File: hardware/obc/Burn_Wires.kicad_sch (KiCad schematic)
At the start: 28 parts, among them Q501 MMBT2222AT, Q502 IRLML2803, Q503 IRLML2803, Q504 IRLML2803, Q505 IRF7406PbF, Q506 IRF7406PbF, Q507 IRF7406PbF, U501 PE014006

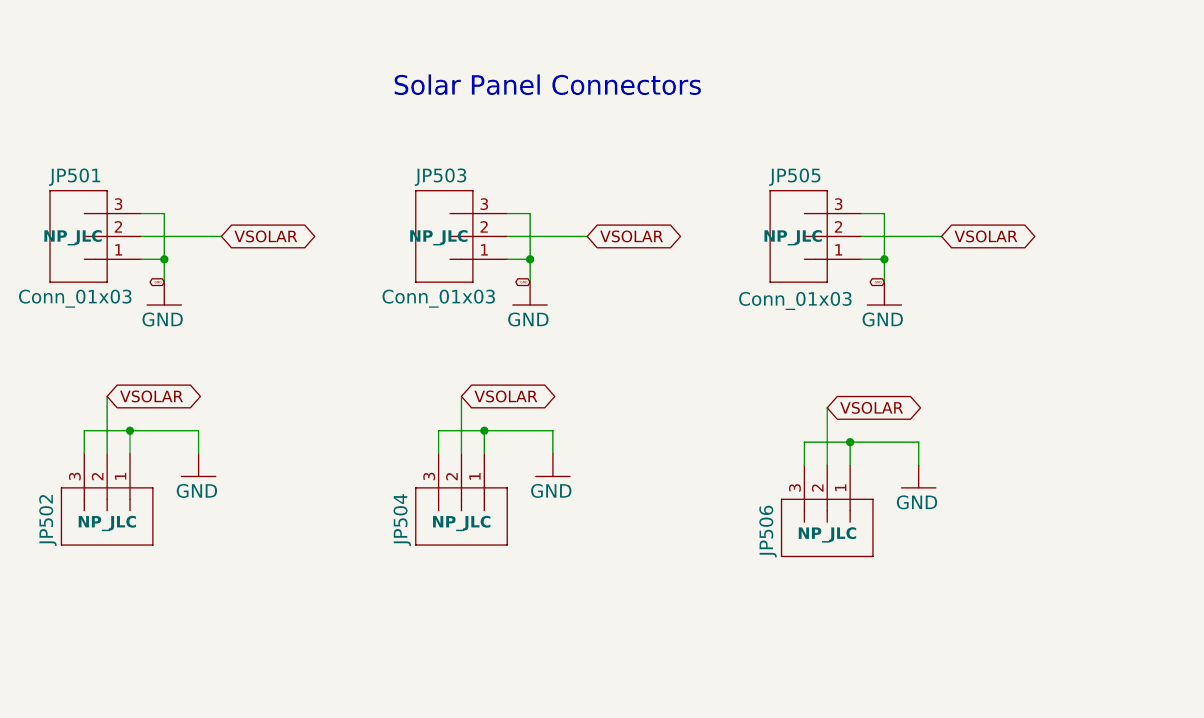
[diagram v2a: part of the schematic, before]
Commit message: OBC; Added another solar charger
- completed all RP2350B decoupling
- added all footprints for new parts
- created a new sheet for all solar charging components
	- added another solar chager to accomadate more voltage from solar pannels
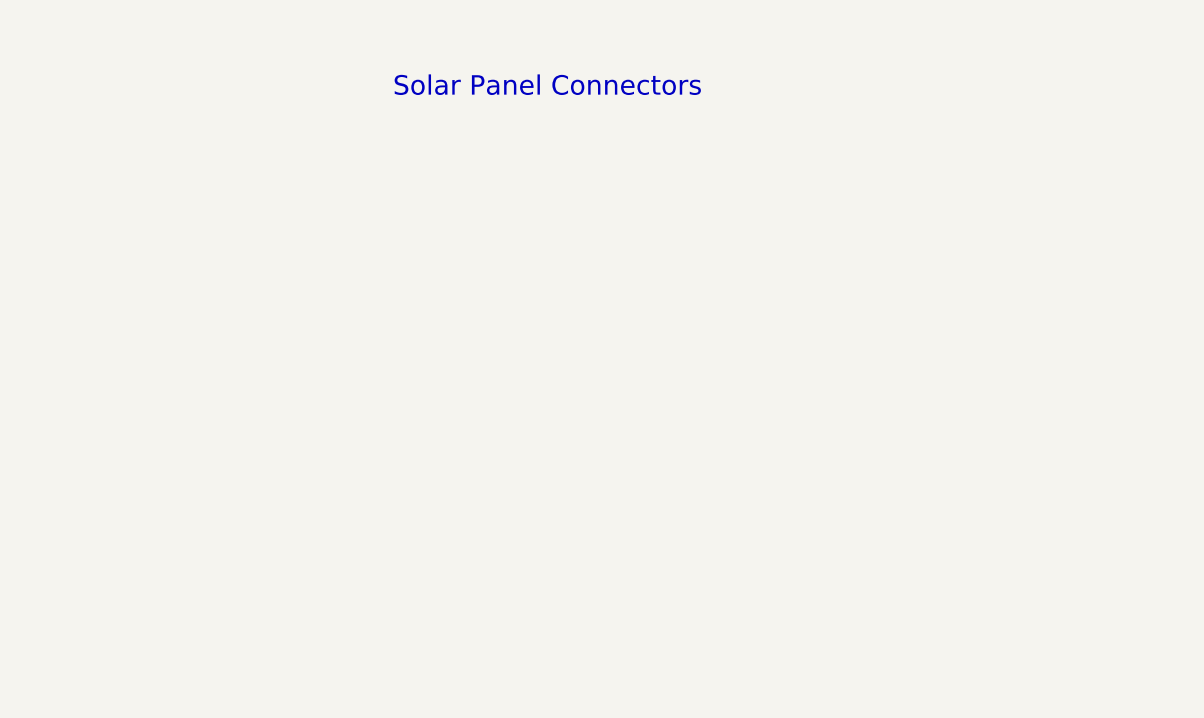
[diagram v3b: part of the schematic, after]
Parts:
- removed JP501, JP502, JP503, JP504, JP505, JP506: Conn_01x03, SSE_Footprints:CONN_22-11-2032_MOL, symbol mainboard:M03POLAR_LOCK

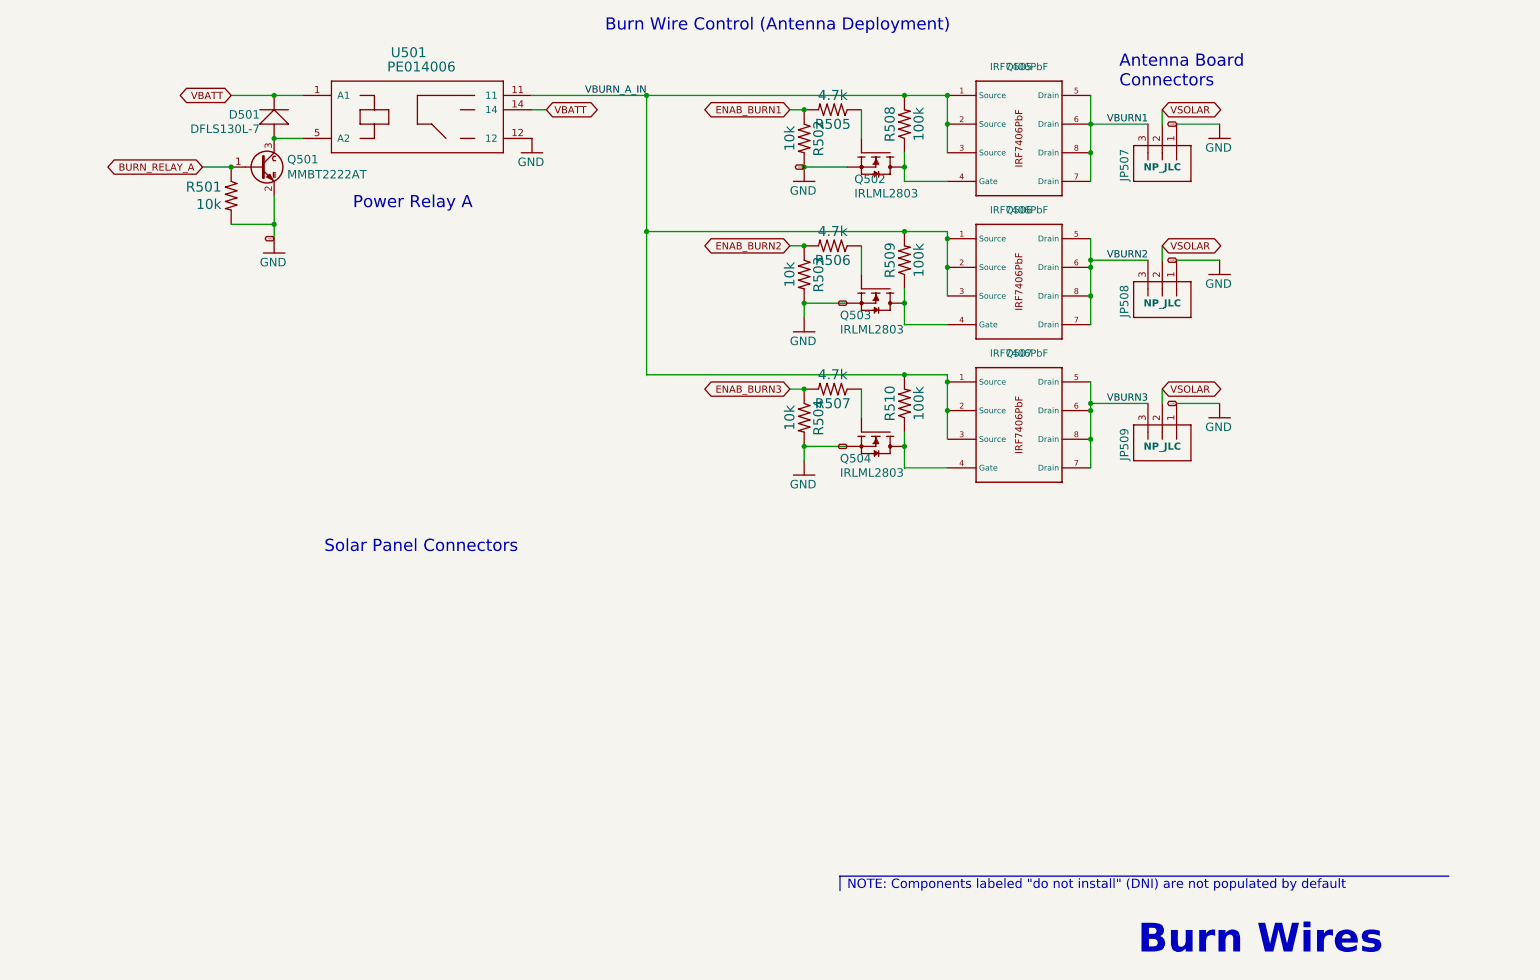
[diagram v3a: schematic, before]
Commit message: OBC: Continuing work towards the next revision
- moved Jtag to Avionics page
- re-aligned and removed excess text
- flipped watchdog to make +3.3v face up
- cleaned up VREG pins, crystal, SWCLK, SWDIO, and watch dog connections
- fixed MRAM symbol
- changed USB_D +/- resistor values
- spaced out schematics on power and burn wire pages
- fixed GNDREF connection for J302
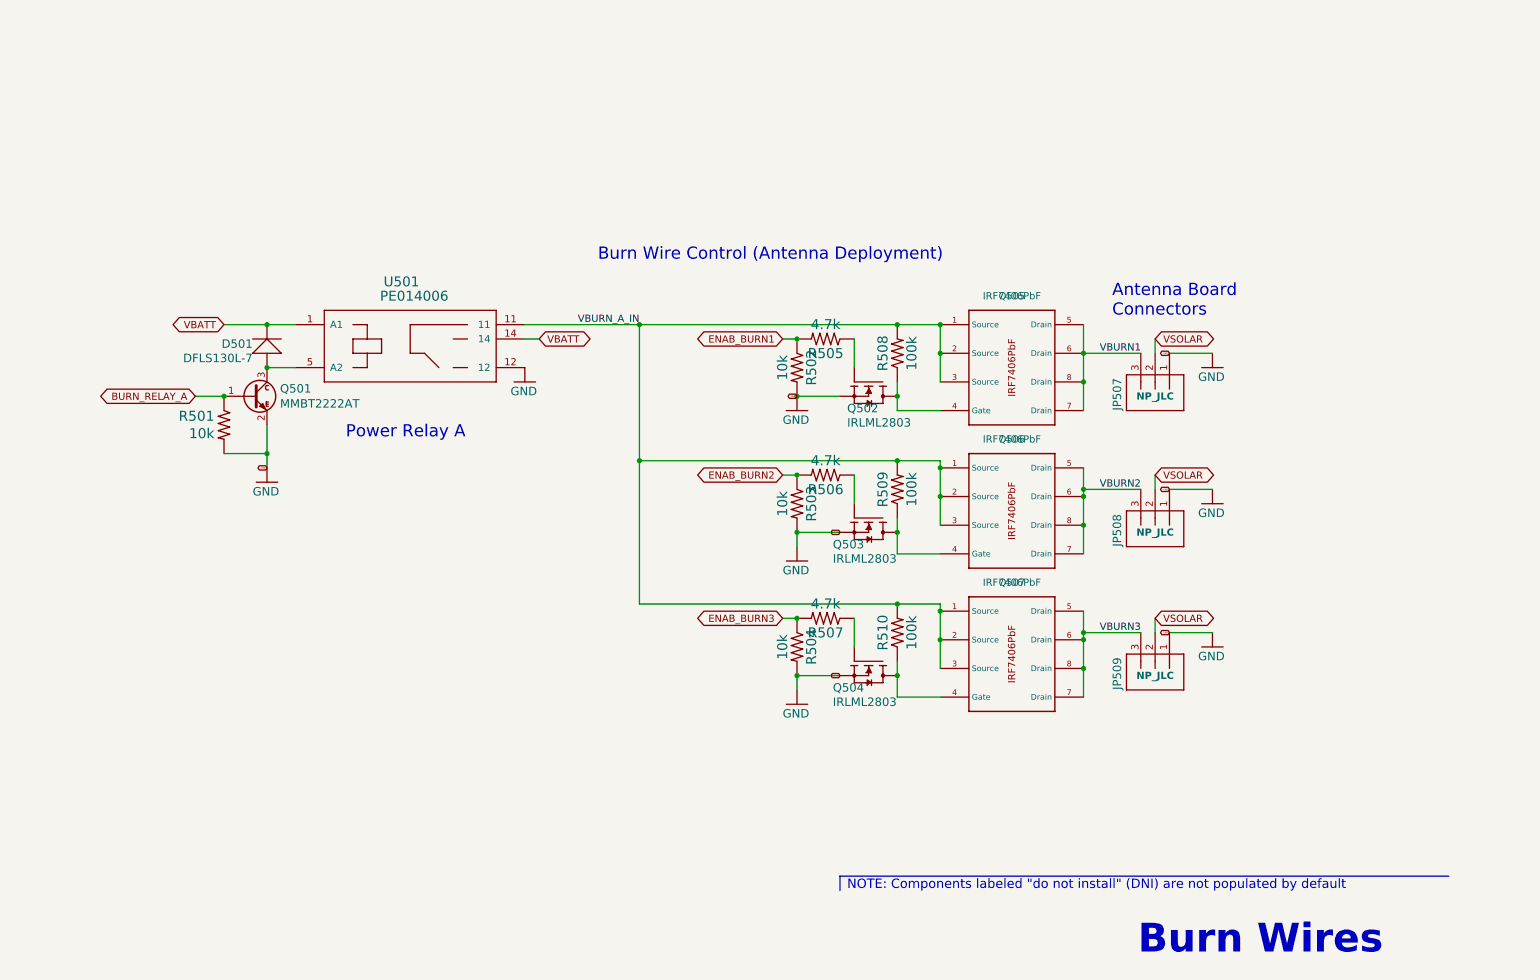
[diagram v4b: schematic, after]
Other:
- note removed: "Solar Panel Connectors"
- moved on the sheet: D501, JP507, JP508, JP509, Q501, Q502, Q503, Q504, Q505, Q506, Q507, R501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

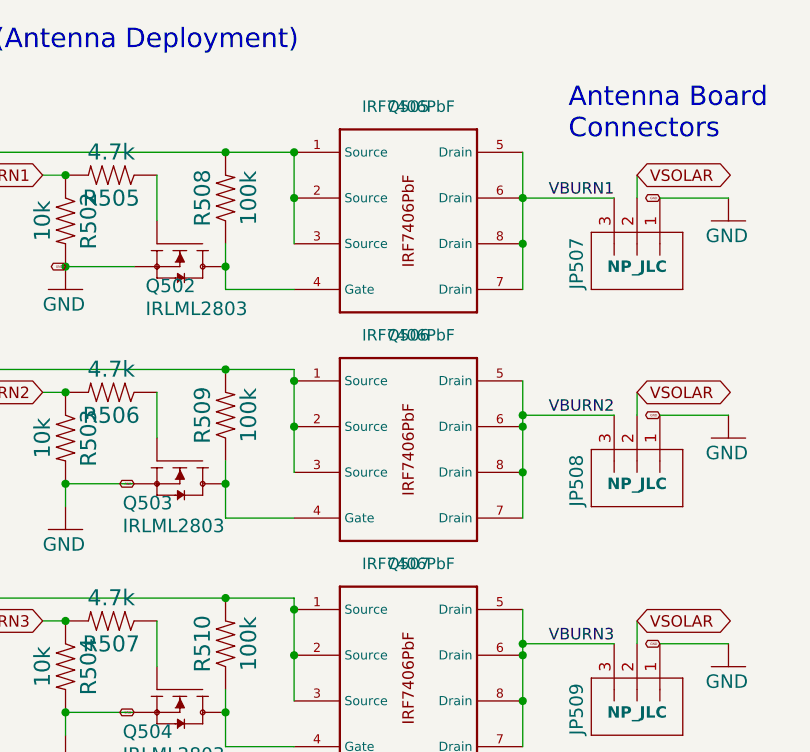
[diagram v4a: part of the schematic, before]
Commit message: OBC: Continuing work towards the next revision
- Changed 3.3V names on Avionics page
- Removed buss protection-bypass jumpers
- Edited SPI buss protection
- Removed U302
- Removed JP401
- Other label/clean up modifications
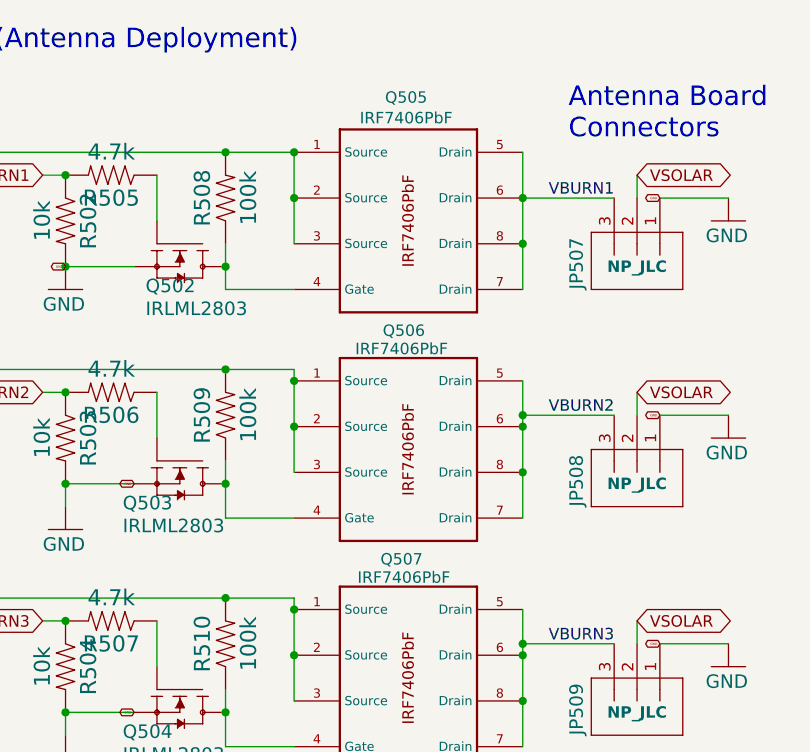
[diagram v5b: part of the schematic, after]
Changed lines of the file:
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@@
 		(on_board yes)
 		(dnp no)
-		(fields_autoplaced yes)
 		(property "Reference" "Q506"
-			(at 189.23 91.44 0)
+			(at 188.722 90.932 0)
 			(effects
 				(font
@@
 		)
 		(property "Value" "IRF7406PbF"
-			(at 189.23 91.44 0)
+			(at 188.468 92.964 0)
 			(effects
 				(font
@@
 		(on_board yes)
 		(dnp no)
-		(fields_autoplaced yes)
 		(property "Reference" "Q505"
-			(at 189.23 66.04 0)
+			(at 188.976 65.024 0)
 			(effects
 				(font
@@
 		)
 		(property "Value" "IRF7406PbF"
-			(at 189.23 66.04 0)
+			(at 188.976 67.31 0)
 			(effects
 				(font
@@
 		(on_board yes)
 		(dnp no)
-		(fields_autoplaced yes)
 		(property "Reference" "Q507"
-			(at 189.23 116.84 0)
+			(at 188.468 116.332 0)
 			(effects
 				(font
@@
 		)
 		(property "Value" "IRF7406PbF"
-			(at 189.23 116.84 0)
-			(effects
-				(font
+			(at 188.722 118.364 0)
+			(effects
+				(font

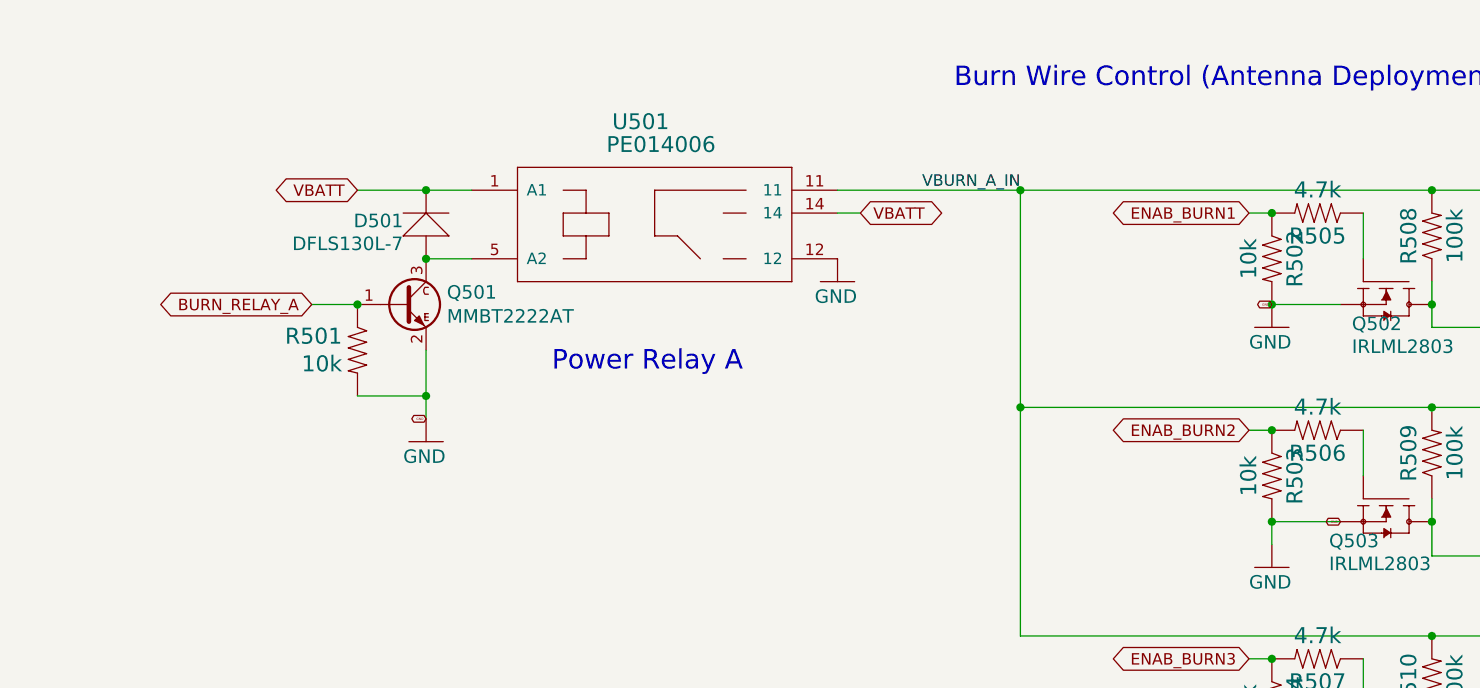
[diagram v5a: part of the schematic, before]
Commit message: OBC: Continuing work towards the next revision
- Cleaned up text on Avionics Page
- Changed some descriptions and cleaned up text on Power Page
- Changed Power Relay A schematic to one from PCB
- Changed R120 and R401 changed from 107k to 34.8k and changed R121 and R404 from 0 to 10k and R127 and R419 from 3.01k to 3.83k (Solar Chargers Page)
- Checked R303 and R304 resistor value and believe 27 is correct
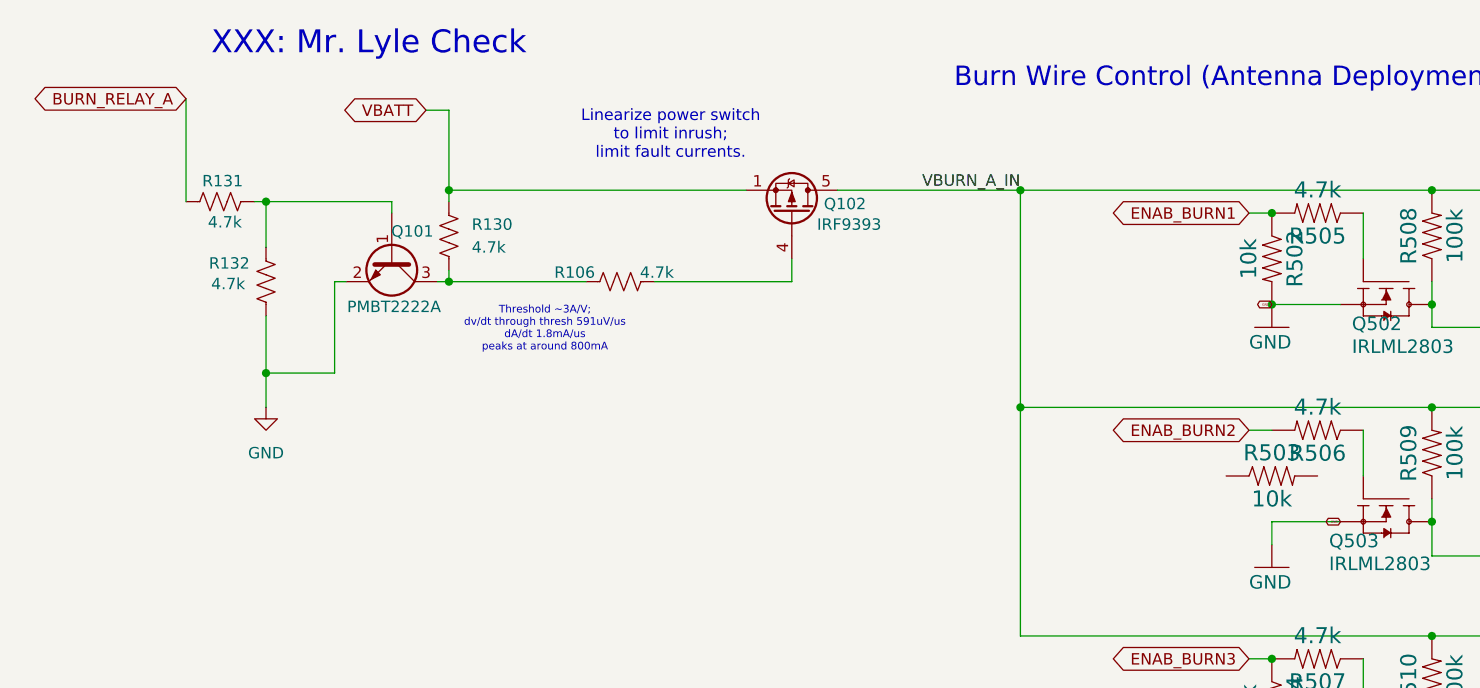
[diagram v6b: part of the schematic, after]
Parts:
- removed D501: DFLS130L-7, Diode_SMD:D_SOD-123, symbol mainboard:DFLS130L
- removed Q501: MMBT2222AT, mainboard:SOT-23, symbol mainboard:MMBT2222AT
- removed R501: 10k, Resistor_SMD:R_0603_1608Metric, symbol mainboard:RESISTOR0603
- removed U501: PE014006, SSE_Footprints:RELAY_PE014006_REV-SSE, symbol mainboard:PE014005
- added Q101: PMBT2222A, Package_TO_SOT_SMD:SOT-23, symbol Transistor_BJT:PMBT2222A
- added Q102: IRF9393, Package_SO:SOIC-8_3.9x4.9mm_P1.27mm, symbol Transistor_FET:IRF7404
- added R106, R130, R131, R132: 4.7k, symbol Device:R_US
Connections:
- net BURN_RELAY_A: now also R131.2
- net ENAB_BURN2: no longer R503.1
- net GND: now also Q101.2 (E), R132.1; no longer R503.2
- net VBATT: now also Q102.1 (S), Q102.2 (S), Q102.3 (S), R130.2
- net VBURN_A_IN: now also Q102.5 (D), Q102.6 (D), Q102.7 (D), Q102.8 (D)
- new net: Q101.3 (C), R106.1, R130.1
- new net: Q102.4 (G), R106.2
- new net: Q101.1 (B), R131.1, R132.2
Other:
- note added: "Linearize power switch to limit inrush; limit fault currents."
- note added: "Threshold ~3A/V; dv/dt through thresh 591uV/us dA/dt 1.8mA/us peaks at around 800mA"
- note added: "XXX: Mr. Lyle Check"
- note removed: "Power Relay A"
- moved on the sheet: R503

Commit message: OBC: Freed up GPIO0 and added footprints
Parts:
- R106, R130, R131, R132: footprint (none) -> Resistor_SMD:R_0603_1608Metric
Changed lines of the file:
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@@
 			)
 		)
-		(property "Footprint" ""
+		(property "Footprint" "Resistor_SMD:R_0603_1608Metric"
 			(at 78.994 80.264 90)
 			(effects
@@
 			)
 		)
-		(property "Footprint" ""
+		(property "Footprint" "Resistor_SMD:R_0603_1608Metric"
 			(at 34.036 73.406 90)
 			(effects
@@
 			)
 		)
-		(property "Footprint" ""
+		(property "Footprint" "Resistor_SMD:R_0603_1608Metric"
 			(at 58.674 75.946 90)
 			(effects
@@
 			)
 		)
-		(property "Footprint" ""
+		(property "Footprint" "Resistor_SMD:R_0603_1608Metric"
 			(at 38.354 81.026 90)
 			(effects

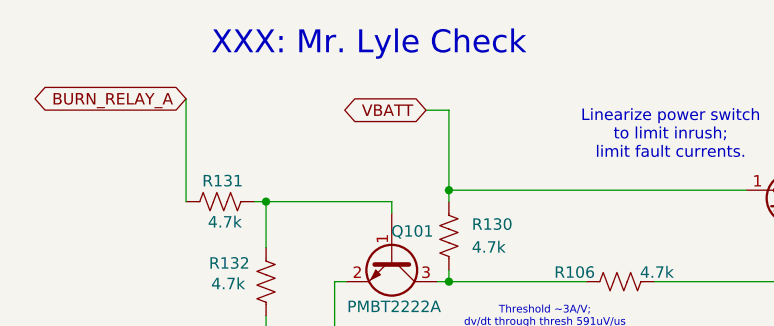
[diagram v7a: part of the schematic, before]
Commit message: obc: Fixed errors from design review
- Gave proper attribution on all pages
- Spread out components on Avionics page
- Changed GPS power circuit
- Added a DNP resistor in between VBATT and VWATCHEDRAIL
- Added various other part numbers on Power Supervisor and Watch Dog Page
- Changed Power Supervisor and Watch Dog Page to page 3
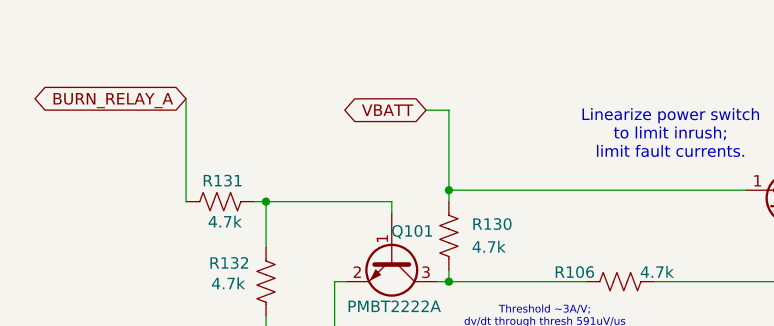
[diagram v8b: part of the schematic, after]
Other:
- note removed: "XXX: Mr. Lyle Check"
- company: Ruchir Kavulli, Michael Lyle -> Ruchir Kavulli, Luke Titi, Michael Lyle
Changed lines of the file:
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@@
 		(date "2024-06-07")
 		(rev "1")
-		(company "Ruchir Kavulli, Michael Lyle")
+		(company "Ruchir Kavulli, Luke Titi, Michael Lyle")
 		(comment 1 "Derived from PyCubed Mainboard v5")
 	)
@@
 		)
 	)
-	(text "XXX: Mr. Lyle Check"
-		(exclude_from_sim no)
-		(at 50.8 54.864 0)
-		(effects
-			(font
-				(size 2.54 2.54)
-			)
-		)
-	)
